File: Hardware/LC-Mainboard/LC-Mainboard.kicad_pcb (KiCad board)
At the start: 2 copper layers, 114.5 x 86.1 mm, 46 parts, among them J1 Raspberry_Pi, J10 Port Enc., J2 Charge Controller, J3 I²C, J4 Beacon, J5 Star.Motor, J6 Port Motor, J7 DC In, J8 PTT, J9 Star.Enc.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

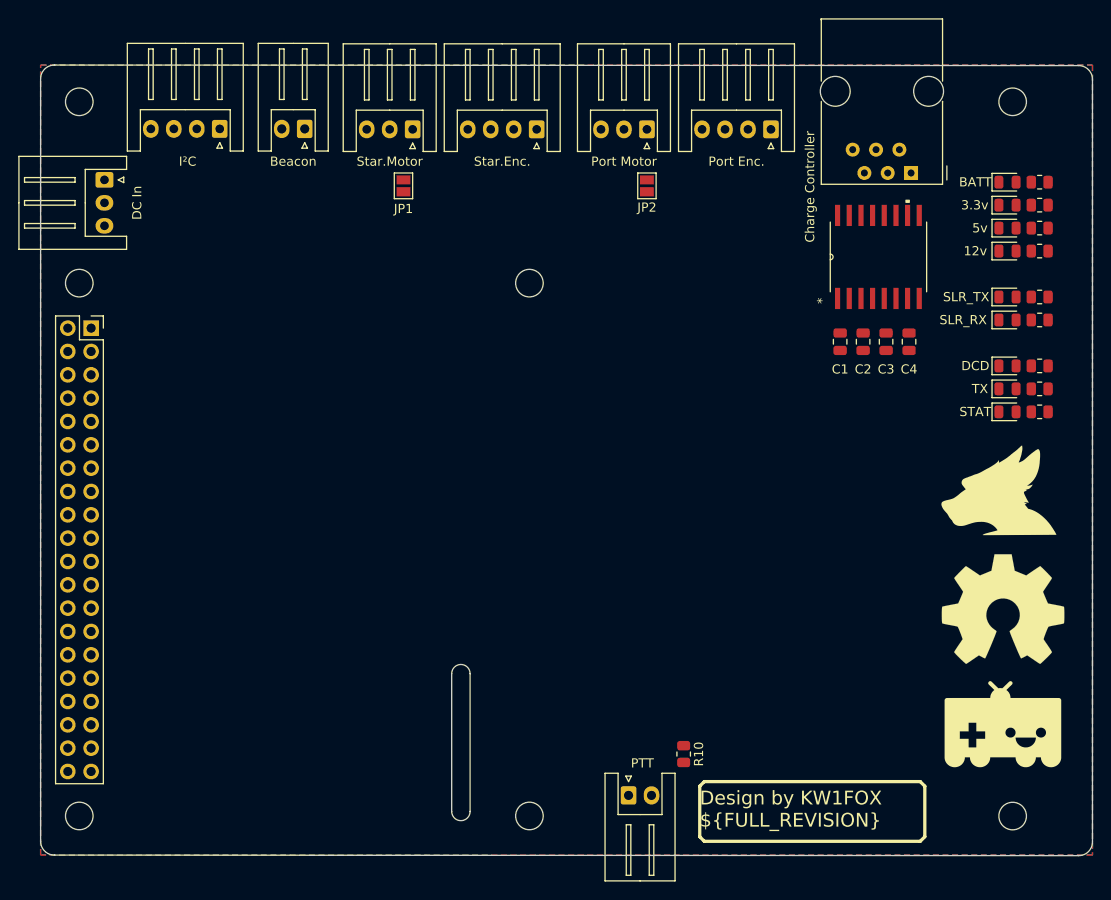
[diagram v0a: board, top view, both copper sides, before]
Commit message: fixup! Rearrange holes
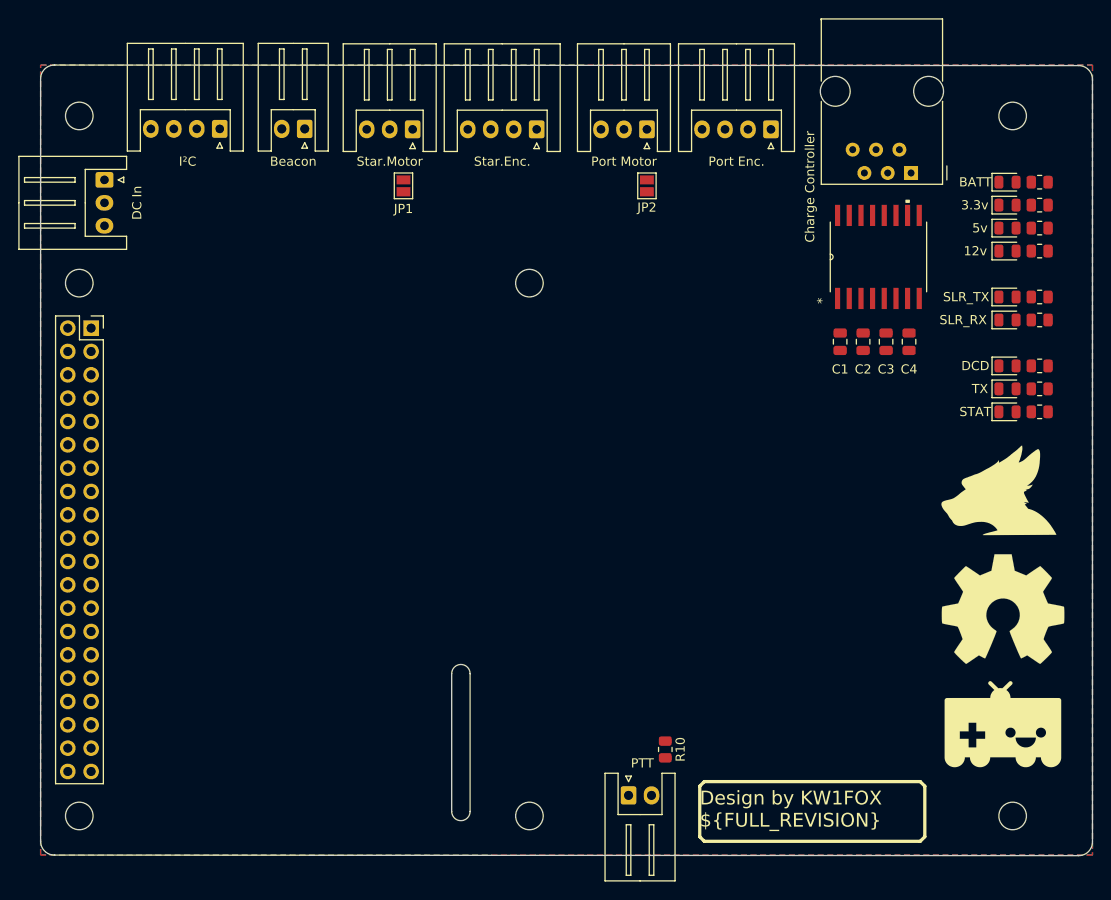
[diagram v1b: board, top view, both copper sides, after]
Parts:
- moved R10 2.06 mm to (171.5, 123.0)
- moved H5 1.54 mm to (107.7, 54.0)
- moved H7 1.54 mm to (209.3, 54.0)
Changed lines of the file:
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@@
   )
   (footprint "Resistor_SMD:R_0805_2012Metric" (layer "F.Cu")
-    (at 173.5 123.5 -90)
+    (at 171.5 123 -90)
     (descr "Resistor SMD 0805 (2012 Metric), square (rectangular) end terminal, IPC_7351 nominal, (Body size source: IPC-SM-782 page 72, https://www.pcb-3d.com/wordpress/wp-content/uploads/ipc-sm-782a_amendment_1_and_2.pdf), generated with kicad-footprint-generator")
     (tags "resistor")
@@
   )
   (footprint "MountingHole:MountingHole_3mm" (layer "F.Cu")
-    (at 209.31 130.25)
+    (at 209.31 130.24)
     (descr "Mounting Hole 3mm, no annular")
     (tags "mounting hole 3mm no annular")
@@
   )
   (footprint "MountingHole:MountingHole_3mm" (layer "F.Cu")
-    (at 107.71 52.5)
+    (at 107.71 54.04)
     (descr "Mounting Hole 3mm, no annular")
     (tags "mounting hole 3mm no annular")
@@
   )
   (footprint "MountingHole:MountingHole_3mm" (layer "F.Cu")
-    (at 209.31 52.5)
+    (at 209.31 54.04)
     (descr "Mounting Hole 3mm, no annular")
     (tags "mounting hole 3mm no annular")
@@
     (effects (font (size 1.5 1.5) (thickness 0.3)) (justify left))
   )
+  (dimension (type aligned) (layer "Cmts.User")
+    (pts (xy 209.31 54.04) (xy 209.31 130.24))
+    (height -19.69)
+    (gr_text "3.0000 in" (at 227.85 92.14 90) (layer "Cmts.User")
+      (effects (font (size 1 1) (thickness 0.15)))
+    )
+    (format (units 3) (units_format 1) (precision 4))
+    (style (thickness 0.15) (arrow_length 1.27) (text_position_mode 0) (extension_height 0.58642) (extension_offset 0.5) keep_text_aligned)
+  )
+  (dimension (type aligned) (layer "Cmts.User")
+    (pts (xy 107.71 54.04) (xy 209.31 54.04))
+    (height -23.25)
+    (gr_text "4.0000 in" (at 158.51 29.64) (layer "Cmts.User")
+      (effects (font (size 1 1) (thickness 0.15)))
+    )
+    (format (units 3) (units_format 1) (precision 4))
+    (style (thickness 0.15) (arrow_length 1.27) (text_position_mode 0) (extension_height 0.58642) (extension_offset 0.5) keep_text_aligned)
+  )
   (zone (net 24) (net_name "GND") (layers F&B.Cu) (hatch edge 0.508)

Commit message: Most of the routing is patched up, review with dad!
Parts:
- added C5: 10μf, Capacitor_SMD:C_0805_2012Metric, F.Cu at (117.5, 67.0)
- added C6: 10μf, Capacitor_SMD:C_0805_2012Metric, F.Cu at (121.7, 67.0)
- added U2: NCP1117-12_SOT223, Package_TO_SOT_SMD:SOT-223-3_TabPin2, F.Cu at (120.8, 72.8)
- moved JP2 2.50 mm to (167.0, 61.6)
- moved JP1 1.50 mm to (141.5, 61.6)
- moved R10 1.50 mm to (170.0, 123.0)
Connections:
- D9 pad 1: TX_LED -> PTT
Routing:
- net +3V3: track 0.00 -> 167.0 mm
- net +5V: track 0.00 -> 161.3 mm, vias 0 -> 2
- net PTT: track 0.00 -> 145.4 mm
- net PI_TX: track 0.00 -> 125.3 mm, vias 0 -> 2
- net +12V: track 0.00 -> 120.1 mm, vias 0 -> 1
- net STAT_LED: track 0.00 -> 118.3 mm, vias 0 -> 1
- net PI_RX: track 0.00 -> 117.1 mm, vias 0 -> 2
- net PORT_PWM: track 0.00 -> 117.1 mm
- net DCD_LED: track 0.00 -> 108.1 mm
- net +12VA: track 0.00 -> 105.5 mm, vias 0 -> 1
- net STAR_PWM: track 0.00 -> 98.1 mm, vias 0 -> 1
- net SCL: track 0.00 -> 39.5 mm, vias 0 -> 2
- net SDA: track 0.00 -> 37.7 mm
- net REN_RX: track 0.00 -> 9.04 mm
- net Net-(C2-Pad1): track 0.00 -> 8.70 mm
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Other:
- board text added: "Robot Mainboard ${FULL_REVISION} Design by KW1FOX"
- board text removed: "Design by KW1FOX ${FULL_REVISION}"

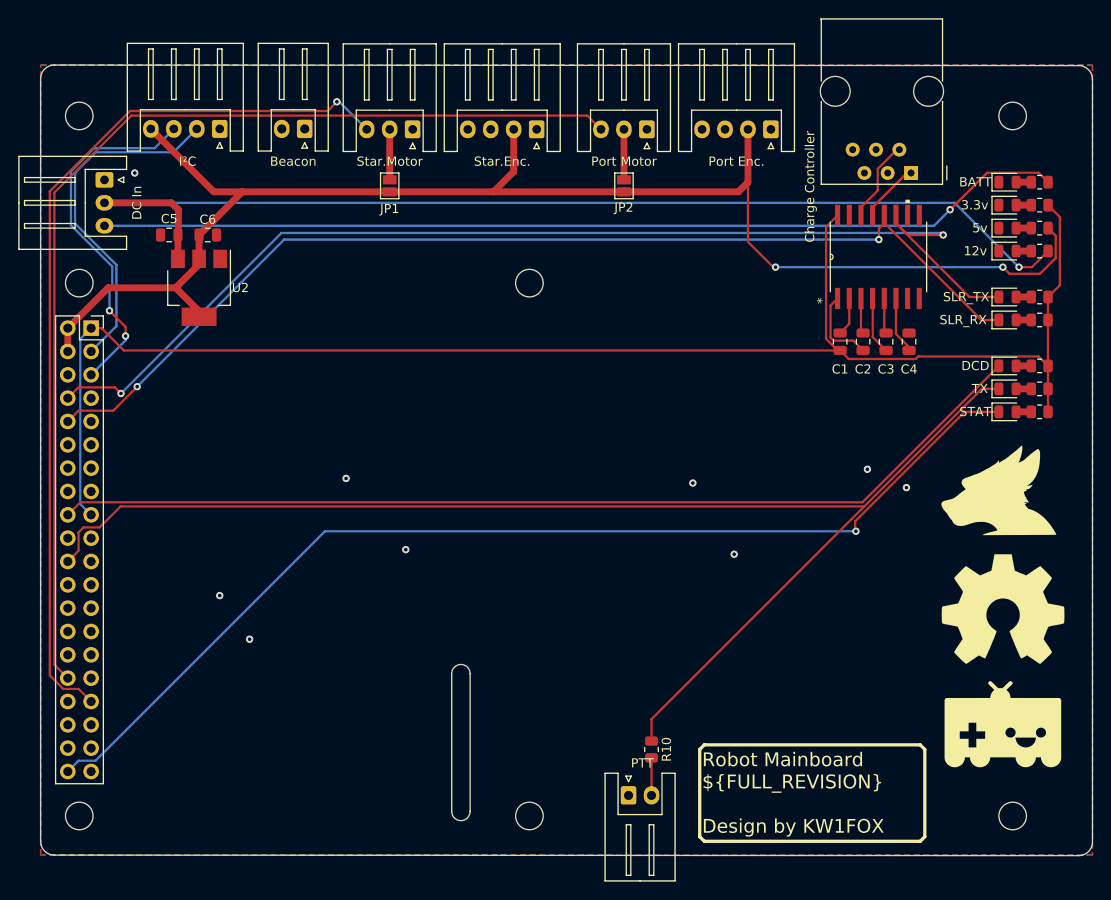
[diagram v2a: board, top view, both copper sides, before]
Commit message: Shrink board size
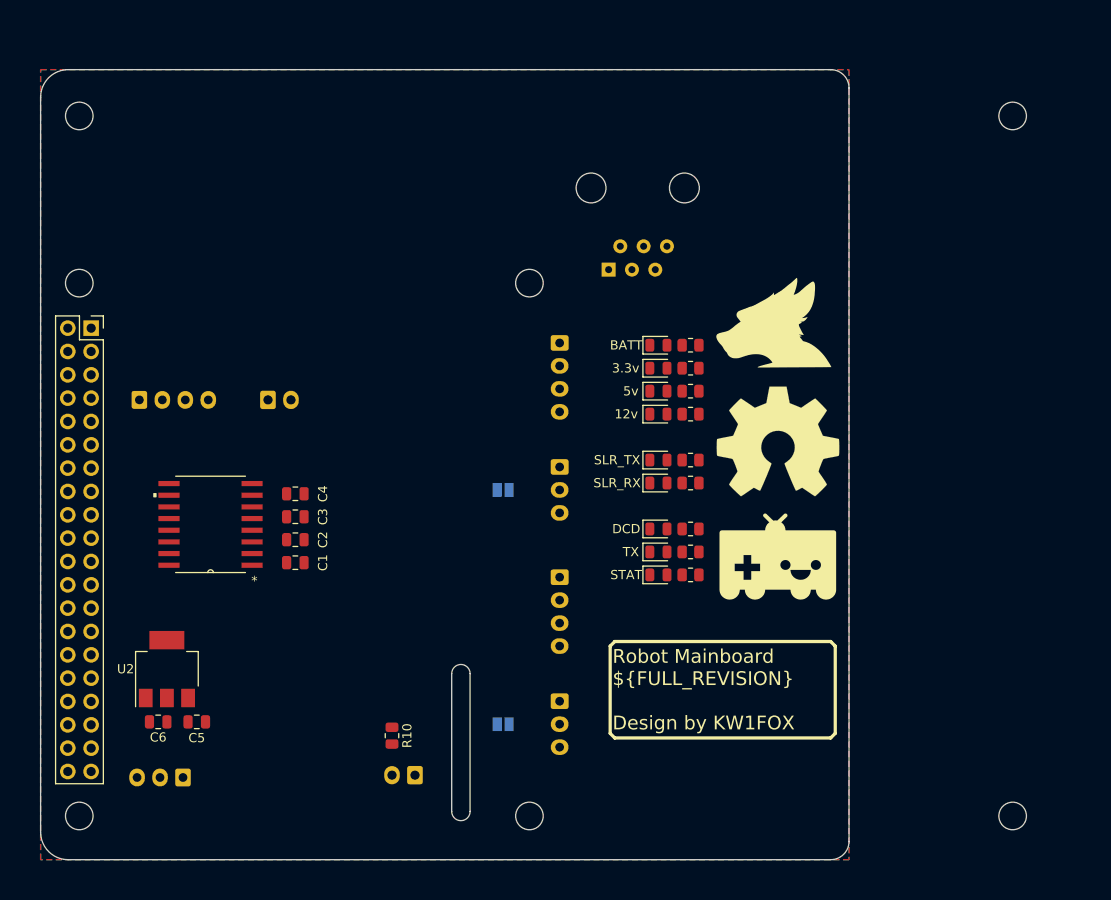
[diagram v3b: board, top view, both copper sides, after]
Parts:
- J10, J2, J3, J4, J5, J6, J7, J8, J9, JP1, JP2: moved to B.Cu
- moved U1 78.3 mm to (122.0, 98.5), turned to 180 degrees
- moved C4 68.8 mm to (131.2, 95.2), turned to 180 degrees
- moved C3 67.1 mm to (131.2, 97.7), turned to 180 degrees
- moved J7 65.6 mm to (119.0, 126.0), turned to 180 degrees
- moved C2 65.5 mm to (131.2, 100.2), turned to 180 degrees
- moved J5 64.3 mm to (160.0, 117.8), turned to -90 degrees
- moved C1 64.0 mm to (131.2, 102.7), turned to 180 degrees
- moved JP1 59.9 mm to (153.8, 120.2), turned to 180 degrees
- moved C6 53.3 mm to (116.3, 120.0), turned to 180 degrees
- moved C5 53.1 mm to (120.5, 120.0), turned to 0 degrees
- moved J9 48.8 mm to (160.0, 104.2), turned to -90 degrees
- moved D1 41.9 mm to (170.8, 94.0)
- moved D2 41.9 mm to (170.8, 91.5)
- moved D3 41.9 mm to (170.8, 86.5)
- moved D4 41.9 mm to (170.8, 84.0)
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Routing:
- net +3V3: track 167.0 -> 0.00 mm
- net +5V: track 161.3 -> 0.00 mm, vias 2 -> 0
- net PTT: track 145.4 -> 0.00 mm
- net PI_TX: track 125.3 -> 0.00 mm, vias 2 -> 0
- net +12V: track 120.1 -> 0.00 mm, vias 1 -> 0
- net STAT_LED: track 118.3 -> 0.00 mm, vias 1 -> 0
- net PI_RX: track 117.1 -> 0.00 mm, vias 2 -> 0
- net PORT_PWM: track 117.1 -> 0.00 mm
- net DCD_LED: track 108.1 -> 0.00 mm
- net +12VA: track 105.5 -> 0.00 mm, vias 1 -> 0
- net STAR_PWM: track 98.1 -> 0.00 mm, vias 1 -> 0
- net SCL: track 39.5 -> 0.00 mm, vias 2 -> 0
- net SDA: track 37.7 -> 0.00 mm
- net REN_RX: track 9.04 -> 0.00 mm
- net Net-(C2-Pad1): track 8.70 -> 0.00 mm
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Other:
- board size 114.5 x 86.1 mm -> 88 x 86 mm

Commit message: Shrink board size even more!
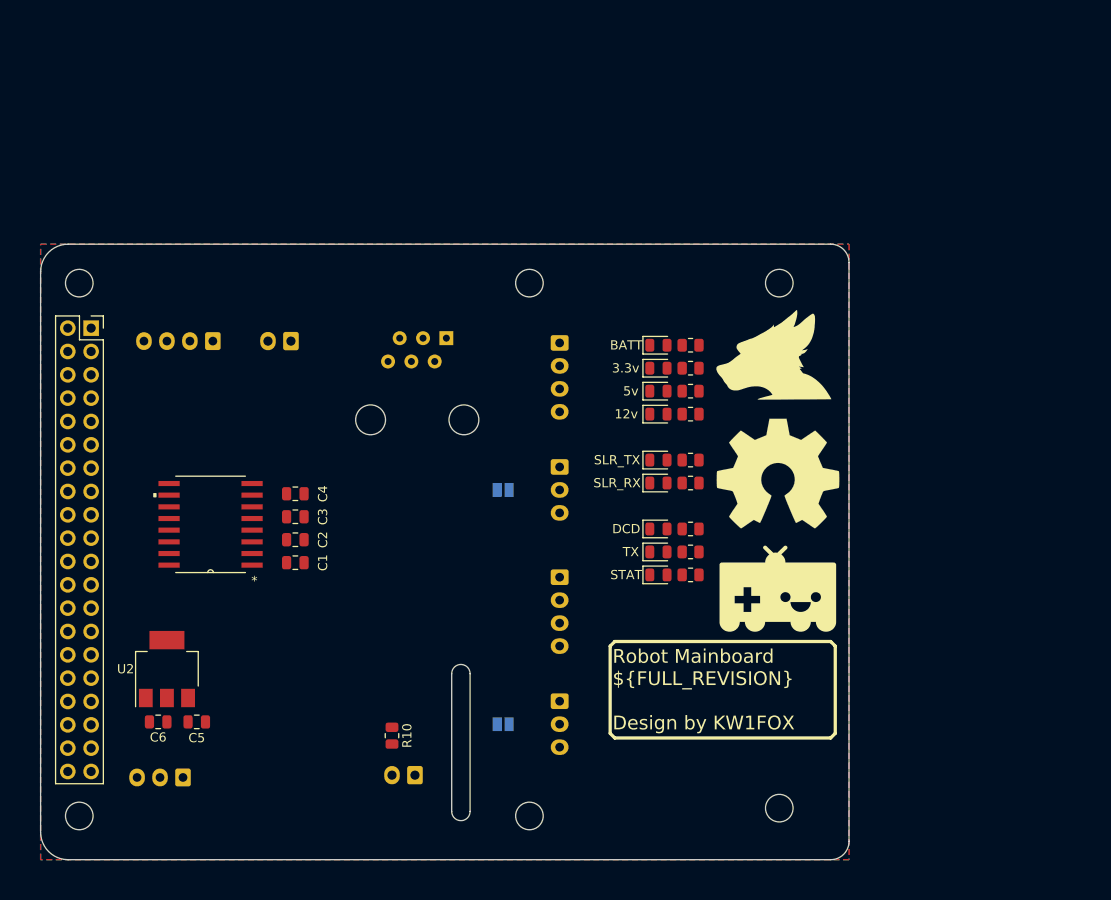
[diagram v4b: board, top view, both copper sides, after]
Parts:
- removed H5: BrdMountingHole, MountingHole:MountingHole_3mm
- moved H7 31.2 mm to (183.9, 72.2)
- moved H6 25.4 mm to (183.9, 129.4)
- moved J2 19.2 mm to (147.7, 78.2), turned to 180 degrees
- moved J3 10.2 mm to (122.2, 78.5), turned to 180 degrees
- moved J4 6.87 mm to (130.8, 78.5), turned to 180 degrees
- moved G*** 3.50 mm to (183.2, 80.0)
- moved G*** 3.50 mm to (183.8, 105.5)
- moved REF** 3.50 mm to (183.8, 93.0)
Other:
- board size 88 x 86 mm -> 88 x 67 mm

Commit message: Add all wiring
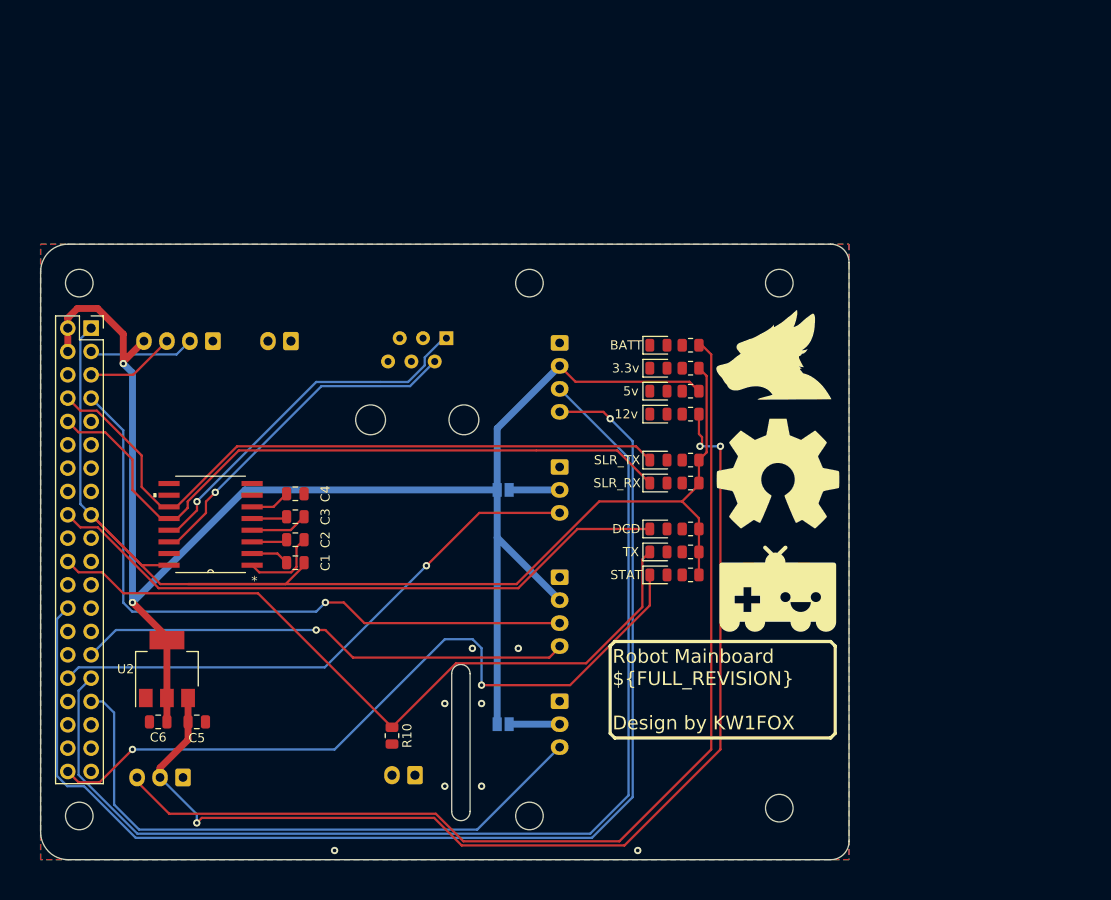
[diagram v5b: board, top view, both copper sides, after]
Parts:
- turned C4 to 0 degrees
- renumbered H7 to H5
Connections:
- J1 pad 26: unconnected-(J1-Pad26) -> PORT_ENC_B
- J1 pad 29: unconnected-(J1-Pad29) -> STAR_ENC_B
- J1 pad 31: unconnected-(J1-Pad31) -> PORT_ENC_A
- J1 pad 7: unconnected-(J1-Pad7) -> STAR_ENC_A
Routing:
- net +5V: track 0.00 -> 171.6 mm, vias 0 -> 2
- net +3V3: track 0.00 -> 141.7 mm
- net PORT_ENC_B: track 0.00 -> 134.1 mm, vias 0 -> 1
- net PORT_ENC_A: track 0.00 -> 122.7 mm
- net +12V: track 0.00 -> 118.3 mm, vias 0 -> 3
- net +12VA: track 0.00 -> 114.5 mm
- net PTT: track 0.00 -> 81.8 mm
- net STAT_LED: track 0.00 -> 81.6 mm, vias 0 -> 2
- net PI_RX: track 0.00 -> 74.6 mm
- net PI_TX: track 0.00 -> 73.6 mm
- net STAR_ENC_A: track 0.00 -> 73.0 mm, vias 0 -> 1
- net DCD_LED: track 0.00 -> 69.3 mm
- net STAR_PWM: track 0.00 -> 66.4 mm
- net PORT_PWM: track 0.00 -> 61.0 mm, vias 0 -> 1
- net STAR_ENC_B: track 0.00 -> 54.0 mm, vias 0 -> 1
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
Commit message: Add almost everything
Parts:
- added Q1: MMBT3906, Package_TO_SOT_SMD:SOT-23, F.Cu at (126.5, 83.0)
- added R11: math, Resistor_SMD:R_0805_2012Metric, F.Cu at (126.5, 86.0)
- added R12: math, Resistor_SMD:R_0805_2012Metric, F.Cu at (126.5, 88.0)
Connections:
- J1 pad 38: unconnected-(J1-Pad38) -> BCON_LED
- J4 pad 2: unconnected-(J4-Pad2) -> BCON_LOAD
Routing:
- net +5V: track 171.6 -> 0.00 mm, vias 2 -> 0
- net +3V3: track 141.7 -> 0.00 mm
- net PORT_ENC_B: track 134.1 -> 0.00 mm, vias 1 -> 0
- net PORT_ENC_A: track 122.7 -> 0.00 mm
- net +12V: track 118.3 -> 2.08 mm, vias 3 -> 0
- net +12VA: track 114.5 -> 0.00 mm
- net PTT: track 81.8 -> 0.00 mm
- net STAT_LED: track 81.6 -> 0.00 mm, vias 2 -> 0
- net PI_RX: track 74.6 -> 0.00 mm
- net PI_TX: track 73.6 -> 0.00 mm
- net STAR_ENC_A: track 73.0 -> 0.00 mm, vias 1 -> 0
- net DCD_LED: track 69.3 -> 0.00 mm
- net STAR_PWM: track 66.4 -> 0.00 mm
- net PORT_PWM: track 61.0 -> 0.00 mm, vias 1 -> 0
- net STAR_ENC_B: track 54.0 -> 0.00 mm, vias 1 -> 0
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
